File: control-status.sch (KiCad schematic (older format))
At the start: 11 parts, among them SW1 SW_PUSH, SW2 SW_PUSH, U10 MAX803

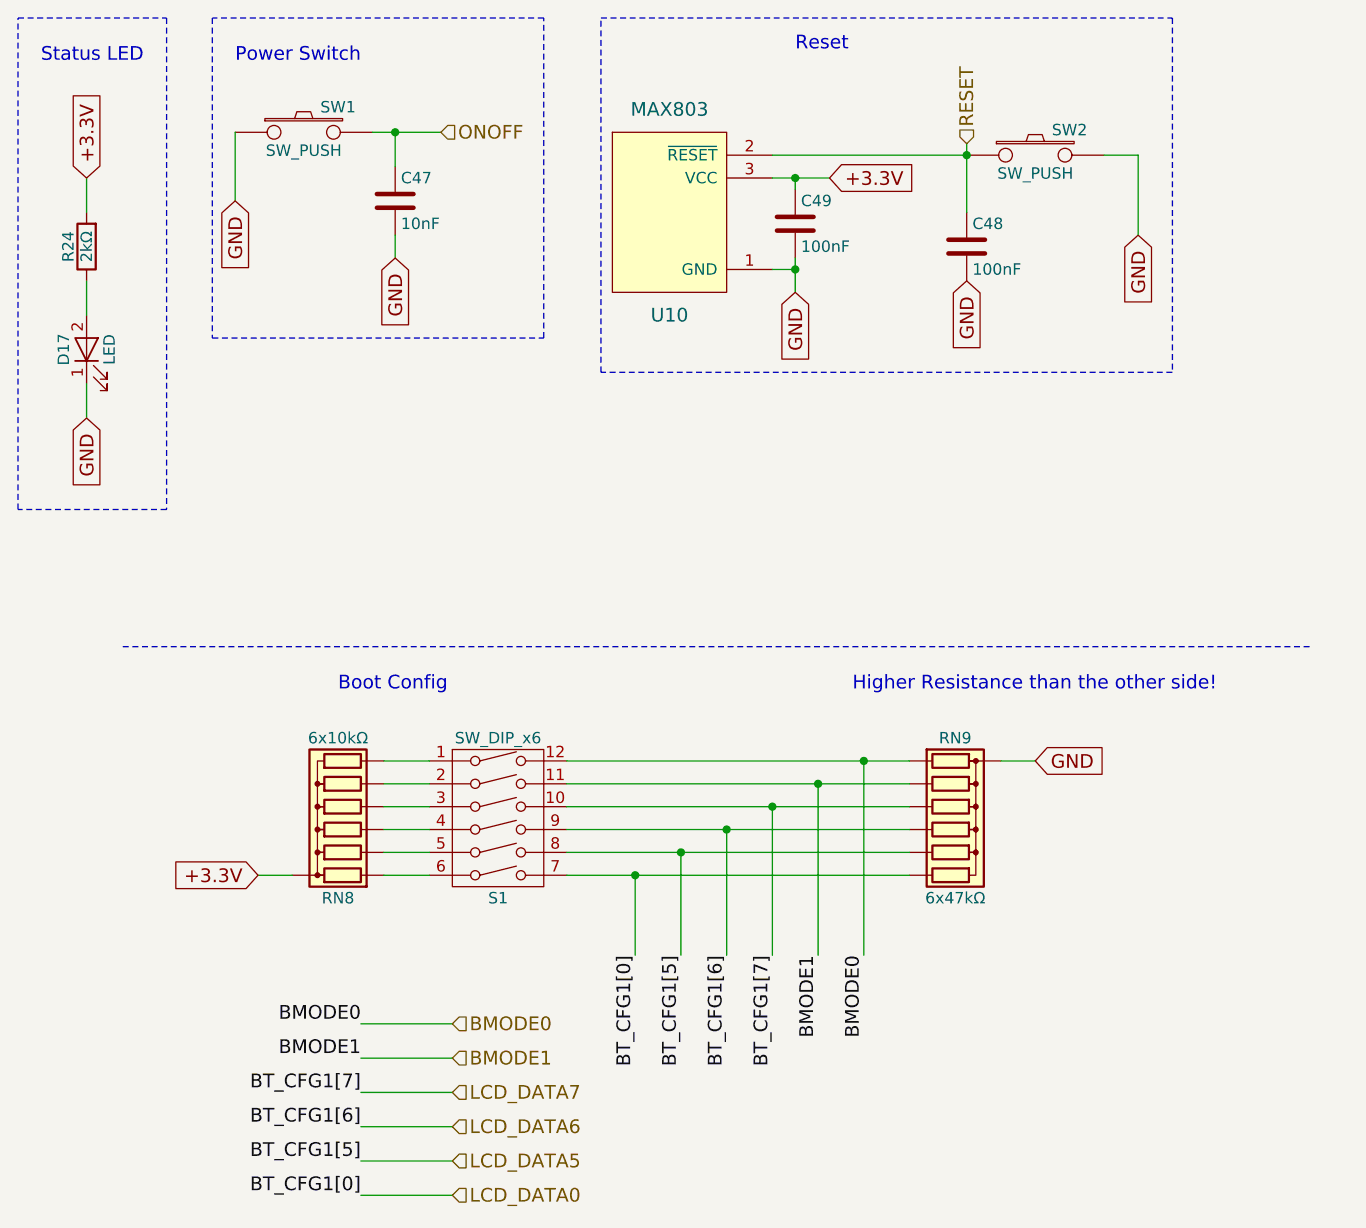
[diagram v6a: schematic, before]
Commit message: I have replaced the 8xresistors to 4resistors because the distance between the pads was not big enough for the 3um copper layers
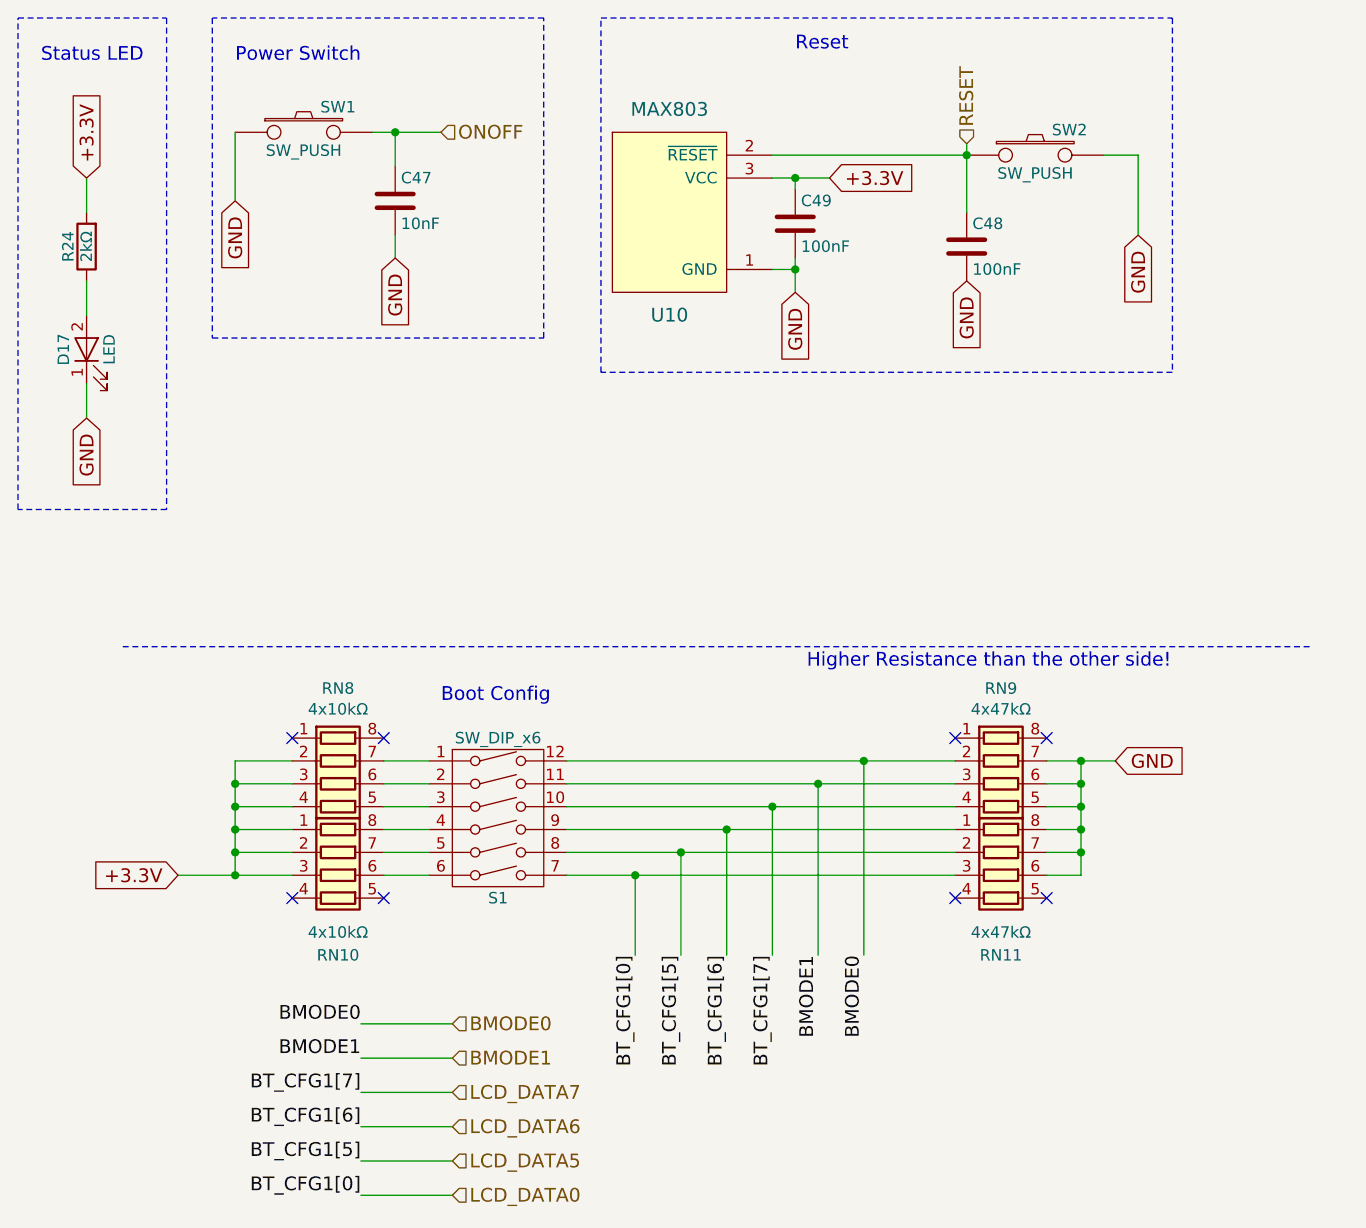
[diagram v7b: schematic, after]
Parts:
- removed RN8: 6x10kΩ, water:YC158-Yageo-Handsoldering, symbol R_Network06
- removed RN9: 6x47kΩ, water:YC158-Yageo-Handsoldering, symbol R_Network06
- added RN10, RN8: 4x10kΩ, kilibs:YC164-Yageo-Handsoldering, symbol R_Pack04
- added RN11, RN9: 4x47kΩ, kilibs:YC164-Yageo-Handsoldering, symbol R_Pack04
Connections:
- net +3.3V: now also RN10.1 (R1.1), RN10.2 (R2.1), RN10.3 (R3.1), RN8.2 (R2.1), RN8.3 (R3.1), RN8.4 (R4.1)
- net BMODE0: now also RN9.2 (R2.1)
- net BMODE1: now also RN9.3 (R3.1)
- net GND: now also RN11.6 (R3.2), RN11.7 (R2.2), RN11.8 (R1.2), RN9.5 (R4.2), RN9.6 (R3.2), RN9.7 (R2.2)
- net LCD_DATA0: now also RN11.3 (R3.1)
- net LCD_DATA5: now also RN11.2 (R2.1)
- net LCD_DATA6: now also RN11.1 (R1.1)
- net LCD_DATA7: now also RN9.4 (R4.1)
- net at S1.1: now also RN8.7 (R2.2)
- net at S1.2: now also RN8.6 (R3.2)
- net at S1.3: now also RN8.5 (R4.2)
- net at S1.4: now also RN10.8 (R1.2)
- net at S1.5: now also RN10.7 (R2.2)
- net at S1.6: now also RN10.6 (R3.2)
- no-connect marks 0 -> 8
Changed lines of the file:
@@
 	1    0    0    -1
 $EndComp
-$Comp
-L R_Network06 RN8
-U 1 1 59A4135A
-P 2150 4200
-F 0 "RN8" V 1750 4200 50  0000 C CNN
-F 1 "6x10kΩ" V 2450 4200 50  0000 C CNN
-F 2 "water:YC158-Yageo-Handsoldering" V 2525 4200 50  0001 C CNN
-F 3 "http://hu.farnell.com/yageo-phycomp/yc158tjr-0710kl/resistor-array-8-10k-0-05-smd/dp/9236236" H 2150 4200 50  0001 C CNN
-	1    2150 4200
-	0    -1   -1   0
-$EndComp
-Text GLabel 1800 4500 0    60   Input ~ 0
+Text GLabel 1450 4500 0    60   Input ~ 0
 +3.3V
 Text HLabel 2650 5150 2    60   Input ~ 0
@@
 Text HLabel 2650 5300 2    60   Input ~ 0
 BMODE1
-Text GLabel 5200 4000 2    60   Input ~ 0
+Text GLabel 5550 4000 2    60   Input ~ 0
 GND
 Text HLabel 2650 5900 2    60   Input ~ 0
@@
 Text HLabel 2650 5450 2    60   Input ~ 0
 LCD_DATA7
-Wire Wire Line
-	1050 1450 1050 1600
-Wire Wire Line
-	1050 1900 1050 2050
-Wire Wire Line
-	1050 2350 1050 2500
-Wire Wire Line
-	1700 1550 1700 1250
-Wire Wire Line
-	2400 1800 2400 1700
-Wire Wire Line
-	2300 1250 2600 1250
-Wire Wire Line
-	2400 1400 2400 1250
-Connection ~ 2400 1250
-Wire Notes Line
-	750  750  1400 750
-Wire Notes Line
-	1400 750  1400 2900
-Wire Notes Line
-	1400 2900 750  2900
-Wire Notes Line
-	750  2900 750  750
-Wire Notes Line
-	1600 750  1600 2150
-Wire Notes Line
-	1600 2150 3050 2150
-Wire Notes Line
-	3050 2150 3050 750
-Wire Notes Line
-	3050 750  1600 750
-Wire Wire Line
-	5500 1350 5650 1350
-Wire Wire Line
-	5650 1350 5650 1700
-Wire Wire Line
-	4050 1350 4900 1350
-Wire Wire Line
-	4150 1800 4150 1950
-Wire Wire Line
-	4900 1300 4900 1600
-Connection ~ 4900 1350
-Wire Wire Line
-	4050 1850 4150 1850
-Connection ~ 4150 1850
-Wire Wire Line
-	4050 1450 4300 1450
-Wire Wire Line
-	4150 1450 4150 1500
-Connection ~ 4150 1450
-Wire Notes Line
-	3300 750  5800 750
-Wire Notes Line
-	5800 750  5800 2300
-Wire Notes Line
-	5800 2300 3300 2300
-Wire Notes Line
-	3300 2300 3300 750
-Wire Wire Line
-	1800 4500 1950 4500
-Wire Wire Line
-	2350 4000 2550 4000
-Wire Wire Line
-	2350 4100 2550 4100
-Wire Wire Line
-	2350 4200 2550 4200
-Wire Wire Line
-	2350 4300 2550 4300
-Wire Wire Line
-	2350 4400 2550 4400
-Wire Wire Line
-	2350 4500 2550 4500
-Wire Wire Line
-	3150 4000 4650 4000
-Wire Wire Line
-	3150 4100 4650 4100
-Wire Wire Line
-	3150 4200 4650 4200
-Wire Wire Line
-	3150 4300 4650 4300
-Wire Wire Line
-	3150 4400 4650 4400
-Wire Wire Line
-	3150 4500 4650 4500
-Text Notes 4400 3700 0    60   ~ 0
+Text Notes 4200 3600 0    60   ~ 0
 Higher Resistance than the other side!
 Text Label 2250 5450 2    60   ~ 0
@@
 Text Label 2250 5900 2    60   ~ 0
 BT_CFG1[0]
-Wire Wire Line
-	2250 5450 2650 5450
-Wire Wire Line
-	2250 5600 2650 5600
-Wire Wire Line
-	2250 5750 2650 5750
-Wire Wire Line
-	2250 5900 2650 5900
 Text Label 3450 4850 3    60   ~ 0
 BT_CFG1[0]
@@
 Text Label 4050 4850 3    60   ~ 0
 BT_CFG1[7]
-Text Notes 2150 3700 0    60   ~ 0
+Text Notes 2600 3750 0    60   ~ 0
 Boot Config
-Wire Notes Line
-	6400 3500 1200 3500
 $Comp
 L C C48
@@
 	0    -1   -1   0
 $EndComp
-$Comp
-L R_Network06 RN9
-U 1 1 59AA2AB9
-P 4850 4300
-F 0 "RN9" V 4450 4300 50  0000 C CNN
-F 1 "6x47kΩ" V 5150 4300 50  0000 C CNN
-F 2 "water:YC158-Yageo-Handsoldering" V 5225 4300 50  0001 C CNN
-F 3 "http://hu.farnell.com/yageo-phycomp/yc158tjr-0747kl/resistor-network-rna310-1206-47k/dp/9236279" H 4850 4300 50  0001 C CNN
-	1    4850 4300
-	0    1    1    0
-$EndComp
 Text Label 2250 5150 2    60   ~ 0
 BMODE0
 Text Label 2250 5300 2    60   ~ 0
 BMODE1
-Wire Wire Line
-	2250 5150 2650 5150
-Wire Wire Line
-	2250 5300 2650 5300
-Wire Wire Line
-	5050 4000 5200 4000
 Text Label 4450 4850 3    60   ~ 0
 BMODE0
 Text Label 4250 4850 3    60   ~ 0
 BMODE1
+$Comp
+L R_Pack04 RN8
+U 1 1 59B175C4
+P 2150 4100
+F 0 "RN8" V 1733 4100 50  0000 C CNN
+F 1 "4x10kΩ" V 1824 4100 50  0000 C CNN
+F 2 "kilibs:YC164-Yageo-Handsoldering" V 2425 4100 50  0001 C CNN
+F 3 "http://hu.farnell.com/yageo-phycomp/yc164-jr-0710kl/resistor-array-arv241-1206-10k/dp/9234560" H 2150 4100 50  0001 C CNN
+	1    2150 4100
+	0    1    1    0
+$EndComp
+$Comp
+L R_Pack04 RN10
+U 1 1 59B17A0F
+P 2150 4500
+F 0 "RN10" V 2500 4500 50  0000 C CNN
+F 1 "4x10kΩ" V 2400 4500 50  0000 C CNN
+F 2 "kilibs:YC164-Yageo-Handsoldering" V 2425 4500 50  0001 C CNN
+F 3 "http://hu.farnell.com/yageo-phycomp/yc164-jr-0710kl/resistor-array-arv241-1206-10k/dp/9234560" H 2150 4500 50  0001 C CNN
+	1    2150 4500
+	0    1    1    0
+$EndComp
+Wire Wire Line
+	1050 1450 1050 1600
+Wire Wire Line
+	1050 1900 1050 2050
+Wire Wire Line
+	1050 2350 1050 2500
+Wire Wire Line
+	1700 1550 1700 1250
+Wire Wire Line
+	2400 1800 2400 1700
+Wire Wire Line
+	2300 1250 2600 1250
+Wire Wire Line
+	2400 1400 2400 1250
+Connection ~ 2400 1250
+Wire Notes Line
+	750  750  1400 750
+Wire Notes Line
+	1400 750  1400 2900
+Wire Notes Line
+	1400 2900 750  2900
+Wire Notes Line
+	750  2900 750  750
+Wire Notes Line
+	1600 750  1600 2150
+Wire Notes Line
+	1600 2150 3050 2150
+Wire Notes Line
+	3050 2150 3050 750
+Wire Notes Line
+	3050 750  1600 750
+Wire Wire Line
+	5500 1350 5650 1350
+Wire Wire Line
+	5650 1350 5650 1700
+Wire Wire Line
+	4050 1350 4900 1350
+Wire Wire Line
+	4150 1800 4150 1950
+Wire Wire Line
+	4900 1300 4900 1600
+Connection ~ 4900 1350
+Wire Wire Line
+	4050 1850 4150 1850
+Connection ~ 4150 1850
+Wire Wire Line
+	4050 1450 4300 1450
+Wire Wire Line
+	4150 1450 4150 1500
+Connection ~ 4150 1450
+Wire Notes Line
+	3300 750  5800 750
+Wire Notes Line
+	5800 750  5800 2300
+Wire Notes Line
+	5800 2300 3300 2300
+Wire Notes Line
+	3300 2300 3300 750
+Wire Wire Line
+	1450 4500 1950 4500
+Wire Wire Line
+	2350 4000 2550 4000
+Wire Wire Line
+	2350 4100 2550 4100
+Wire Wire Line
+	2350 4200 2550 4200
+Wire Wire Line
+	2350 4300 2550 4300
+Wire Wire Line
+	2350 4400 2550 4400
+Wire Wire Line
+	2350 4500 2550 4500
+Wire Wire Line
+	3150 4000 4850 4000
+Wire Wire Line
+	3150 4100 4850 4100
+Wire Wire Line
+	3150 4200 4850 4200
+Wire Wire Line
+	3150 4300 4850 4300
+Wire Wire Line
+	3150 4400 4850 4400
+Wire Wire Line
+	3150 4500 4850 4500
+Wire Wire Line
+	2250 5450 2650 5450
+Wire Wire Line
+	2250 5600 2650 5600
+Wire Wire Line
+	2250 5750 2650 5750
+Wire Wire Line
+	2250 5900 2650 5900
+Wire Notes Line
+	6400 3500 1200 3500
+Wire Wire Line
+	2250 5150 2650 5150
+Wire Wire Line
+	2250 5300 2650 5300
 Wire Wire Line
 	3450 4850 3450 4500
@@
 	4450 4850 4450 4000
 Connection ~ 4450 4000
+Wire Wire Line
+	1950 4400 1700 4400
+Connection ~ 1700 4500
+Wire Wire Line
+	1950 4300 1700 4300
+Connection ~ 1700 4400
+Wire Wire Line
+	1950 4200 1700 4200
+Connection ~ 1700 4300
+Wire Wire Line
+	1950 4100 1700 4100
+Connection ~ 1700 4200
+Wire Wire Line
+	1950 4000 1700 4000
+Connection ~ 1700 4100
+Wire Wire Line
+	1700 4000 1700 4500
+$Comp
+L R_Pack04 RN11
+U 1 1 59B18EB9
+P 5050 4500
+F 0 "RN11" V 5400 4500 50  0000 C CNN
+F 1 "4x47kΩ" V 5300 4500 50  0000 C CNN
+F 2 "kilibs:YC164-Yageo-Handsoldering" V 5325 4500 50  0001 C CNN
+F 3 "http://hu.farnell.com/yageo-phycomp/yc164-jr-0747kl/resistor-array-arv241-1206-47k/dp/9234594" H 5050 4500 50  0001 C CNN
+	1    5050 4500
+	0    1    1    0
+$EndComp
+$Comp
+L R_Pack04 RN9
+U 1 1 59B18F4C
+P 5050 4100
+F 0 "RN9" V 4633 4100 50  0000 C CNN
+F 1 "4x47kΩ" V 4724 4100 50  0000 C CNN
+F 2 "kilibs:YC164-Yageo-Handsoldering" V 5325 4100 50  0001 C CNN
+F 3 "http://hu.farnell.com/yageo-phycomp/yc164-jr-0747kl/resistor-array-arv241-1206-47k/dp/9234594" H 5050 4100 50  0001 C CNN
+	1    5050 4100
+	0    1    1    0
+$EndComp
+Wire Wire Line
+	5550 4000 5250 4000
+Wire Wire Line
+	5400 4000 5400 4500
+Wire Wire Line
+	5400 4100 5250 4100
+Connection ~ 5400 4000
+Wire Wire Line
+	5400 4200 5250 4200
+Connection ~ 5400 4100
+Wire Wire Line
+	5400 4300 5250 4300
+Connection ~ 5400 4200
+Wire Wire Line
+	5400 4400 5250 4400
+Connection ~ 5400 4300
+Wire Wire Line
+	5400 4500 5250 4500
+Connection ~ 5400 4400
+NoConn ~ 5250 3900
+NoConn ~ 4850 3900
+NoConn ~ 2350 3900
+NoConn ~ 1950 3900
+NoConn ~ 1950 4600
+NoConn ~ 2350 4600
+NoConn ~ 4850 4600
+NoConn ~ 5250 4600
 $EndSCHEMATC
